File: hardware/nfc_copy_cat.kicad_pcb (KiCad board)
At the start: 2 copper layers, 40.4 x 43 mm, 39 parts, among them J1 USB_B_Micro, J2 Battery, J3 SWD, J4 NFC Module V3, J5 Conn_01x02, J6 Adafruit NFC 1.0, SW2 Magspoof, SW3 NFC, U1 AP2112K-3.3TRG1, U2 MCP73831-2-OT, U3 TC4424, U4 ATSAMD21E18A

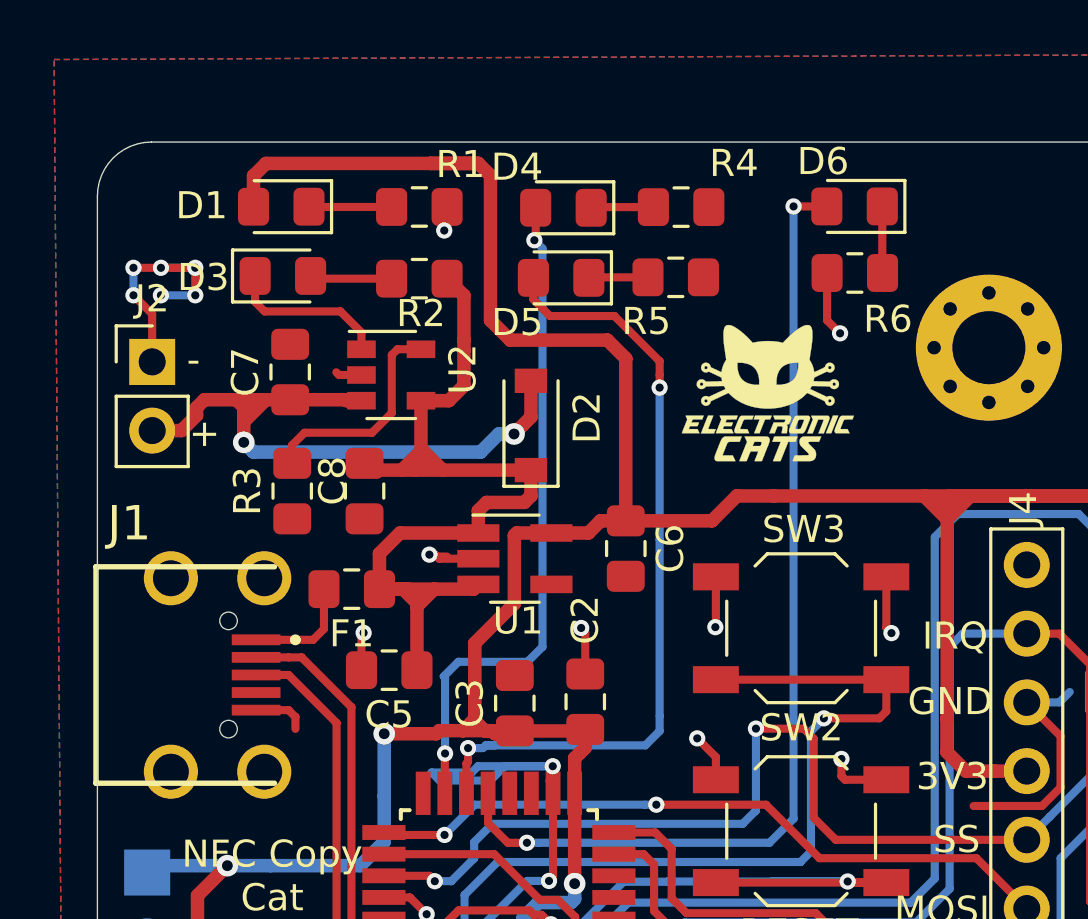
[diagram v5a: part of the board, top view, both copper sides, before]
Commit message: best labels description
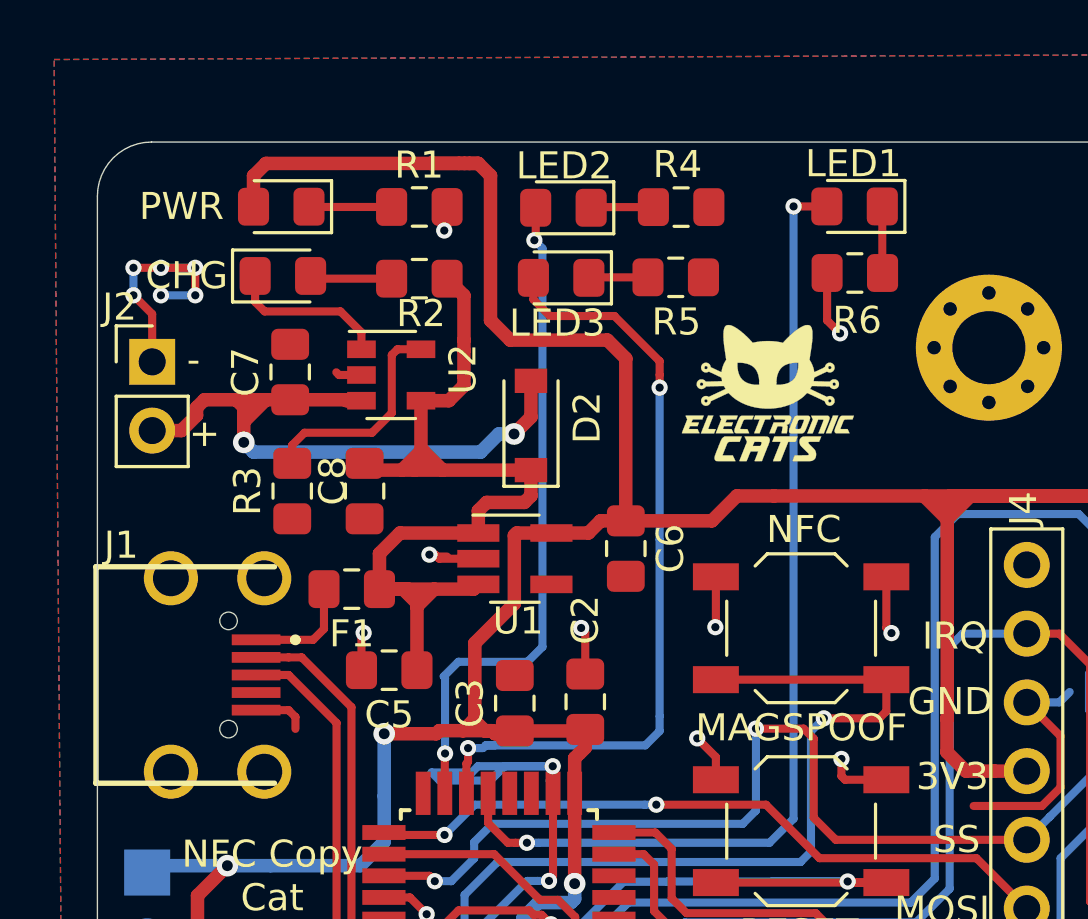
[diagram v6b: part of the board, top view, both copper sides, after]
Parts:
- renumbered D3 to CHG, D6 to LED1, D4 to LED2, D5 to LED3, SW2 to MAGSPOOF, SW3 to NFC, D1 to PWR
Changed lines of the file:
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@@
     (tags "SPST Tactile Switch")
     (attr smd)
-    (fp_text reference SW2 (at -0.01 3.82) (layer F.SilkS)
+    (fp_text reference MAGSPOOF (at -0.01 3.82) (layer F.SilkS)
       (effects (font (size 1 1) (thickness 0.15)))
     )
@@
     (descr U254-051N-4BH806-2)
     (tags Connector)
-    (fp_text reference J1 (at -5.6007 2.5019) (layer F.SilkS)
-      (effects (font (size 1.27 1.27) (thickness 0.254)))
+    (fp_text reference J1 (at -4.7975 2.8015) (layer F.SilkS)
+      (effects (font (size 1 1) (thickness 0.15)))
     )
     (fp_text value USB_B_Micro (at 0 -6.7 270) (layer F.SilkS) hide
@@
     (tags "SPST Tactile Switch")
     (attr smd)
-    (fp_text reference SW3 (at -0.1 3.65 180) (layer F.SilkS)
+    (fp_text reference NFC (at -0.1 3.65 180) (layer F.SilkS)
       (effects (font (size 1 1) (thickness 0.15)))
     )
@@
     (tags "LED handsolder")
     (attr smd)
-    (fp_text reference D1 (at 2.941 0.038) (layer F.SilkS)
+    (fp_text reference PWR (at 3.685 0.01) (layer F.SilkS)
       (effects (font (size 1 1) (thickness 0.15)))
     )
@@
     (tags "LED handsolder")
     (attr smd)
-    (fp_text reference D3 (at -2.941 0.056) (layer F.SilkS)
+    (fp_text reference CHG (at -3.555 -0.01) (layer F.SilkS)
       (effects (font (size 1 1) (thickness 0.15)))
     )
@@
     (descr "Through hole straight pin header, 1x02, 2.54mm pitch, single row")
     (tags "Through hole pin header THT 1x02 2.54mm single row")
-    (fp_text reference J2 (at 0 -2.33) (layer F.SilkS)
+    (fp_text reference J2 (at -1.205 -2.025) (layer F.SilkS)
       (effects (font (size 1 1) (thickness 0.15)))
     )
@@
     (tags "resistor handsolder")
     (attr smd)
-    (fp_text reference R1 (at 1.52 -1.57) (layer F.SilkS)
+    (fp_text reference R1 (at -0.01 -1.55) (layer F.SilkS)
       (effects (font (size 1 1) (thickness 0.15)))
     )
@@
     (tags "LED handsolder")
     (attr smd)
-    (fp_text reference D4 (at 1.715 1.5) (layer F.SilkS)
+    (fp_text reference LED2 (at -0.025 1.55) (layer F.SilkS)
       (effects (font (size 1 1) (thickness 0.15)))
     )
@@
     (tags "resistor handsolder")
     (attr smd)
-    (fp_text reference R4 (at 1.954999 -1.615001) (layer F.SilkS)
+    (fp_text reference R4 (at -0.135001 -1.575001) (layer F.SilkS)
       (effects (font (size 1 1) (thickness 0.15)))
     )
@@
     (tags "LED handsolder")
     (attr smd)
-    (fp_text reference D5 (at 1.62 -1.65) (layer F.SilkS)
+    (fp_text reference LED3 (at 0.14 -1.67) (layer F.SilkS)
       (effects (font (size 1 1) (thickness 0.15)))
     )
@@
     (tags "LED handsolder")
     (attr smd)
-    (fp_text reference D6 (at 1.165 1.66) (layer F.SilkS)
+    (fp_text reference LED1 (at 0.045 1.58) (layer F.SilkS)
       (effects (font (size 1 1) (thickness 0.15)))
     )
@@
     (tags "resistor handsolder")
     (attr smd)
-    (fp_text reference R5 (at -1.085 1.63) (layer F.SilkS)
+    (fp_text reference R5 (at 0.025 1.65) (layer F.SilkS)
       (effects (font (size 1 1) (thickness 0.15)))
     )
@@
     (tags "resistor handsolder")
     (attr smd)
-    (fp_text reference R6 (at -1.225 -1.71) (layer F.SilkS)
-      (effects (font (size 1 1) (thickness 0.15)))
-    )
+    (fp_text reference R6 (at -0.085 -1.75) (layer F.SilkS)
+      (effects (font (size 1 1) (thickness 0.15)))
+    )

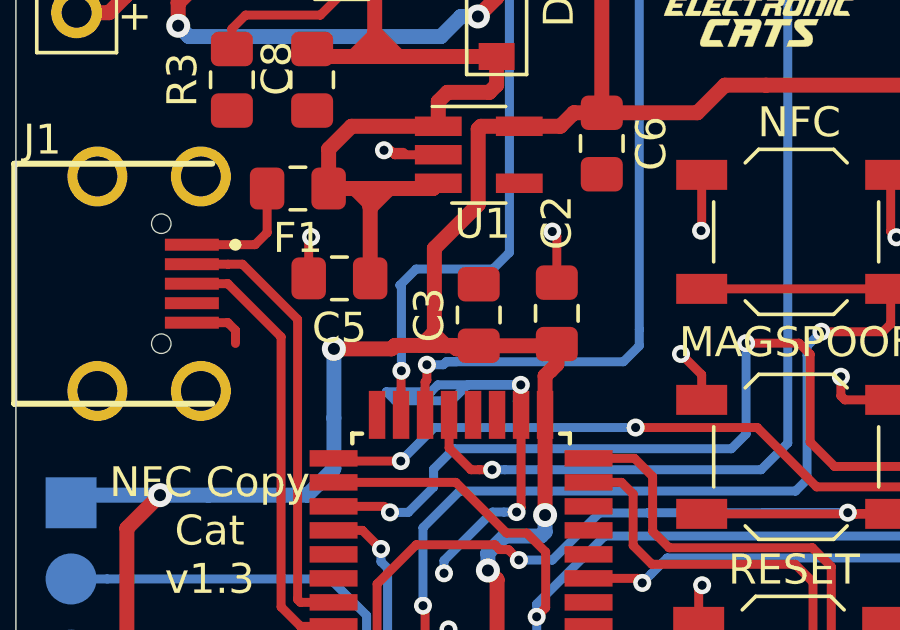
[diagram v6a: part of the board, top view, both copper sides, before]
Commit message: remove c3
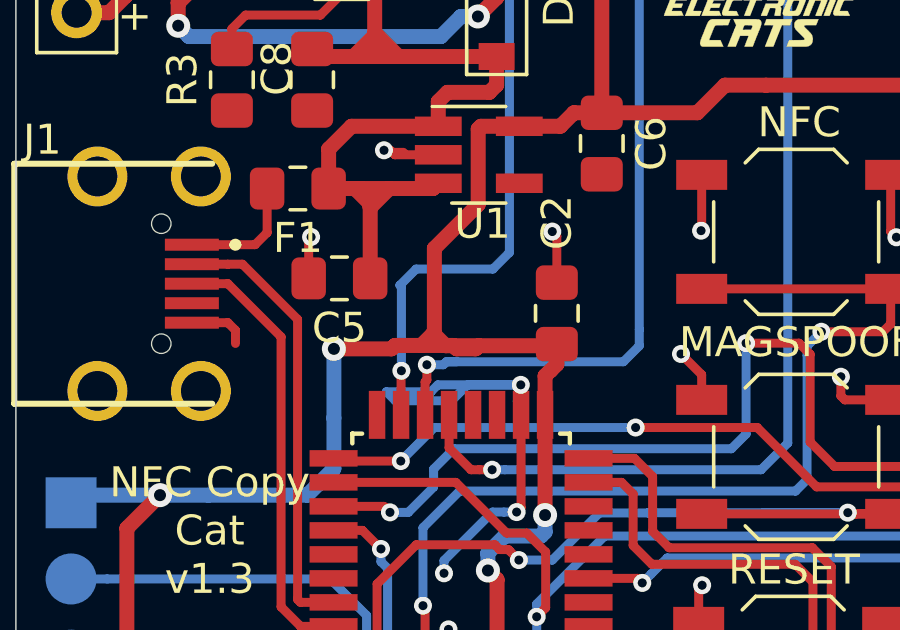
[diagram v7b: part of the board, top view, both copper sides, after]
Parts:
- removed C3: 0.1uf, Capacitor_SMD:C_0805_2012Metric_Pad1.15x1.40mm_HandSolder
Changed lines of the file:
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@@
     (tracks 597)
     (zones 0)
-    (modules 39)
+    (modules 38)
     (nets 49)
   )
@@
       (drillshape 0)
       (scaleselection 1)
-      (outputdirectory "gerbers_nfc/"))
+      (outputdirectory "gerbers_nfc1v3/"))
   )
   (net 0 "")
@@
     (model ${KISYS3DMOD}/Capacitor_SMD.3dshapes/C_0805_2012Metric.wrl
       (at (xyz 0 0 0))
-      (scale (xyz 1 1 1))
-      (rotate (xyz 0 0 0))
-    )
-  )
-  (module Capacitor_SMD:C_0805_2012Metric_Pad1.15x1.40mm_HandSolder (layer F.Cu)
-    (at 143.128 69.941 90)
-    (descr "Capacitor SMD 0805 (2012 Metric), square (rectangular) end terminal, IPC_7351 nominal with elongated pad for handsoldering. (Body size source: https://docs.google.com/spreadsheets/d/1BsfQQcO9C6DZCsRaXUlFlo91Tg2WpOkGARC1WS5S8t0/edit?usp=sharing), generated with kicad-footprint-generator")
-    (tags "capacitor handsolder")
-    (attr smd)
-    (fp_text reference C3 (at 0 -1.65 90) (layer F.SilkS)
-      (effects (font (size 1 1) (thickness 0.15)))
-    )
-    (fp_text value 0.1uf (at 0 1.65 90) (layer F.Fab)
-      (effects (font (size 1 1) (thickness 0.15)))
-    )
-    (fp_line (start -1 0.6) (end -1 -0.6) (layer F.Fab) (width 0.1))
-    (fp_line (start -1 -0.6) (end 1 -0.6) (layer F.Fab) (width 0.1))
-    (fp_line (start 1 -0.6) (end 1 0.6) (layer F.Fab) (width 0.1))
-    (fp_line (start 1 0.6) (end -1 0.6) (layer F.Fab) (width 0.1))
-    (fp_line (start -0.261252 -0.71) (end 0.261252 -0.71) (layer F.SilkS) (width 0.12))
-    (fp_line (start -0.261252 0.71) (end 0.261252 0.71) (layer F.SilkS) (width 0.12))
-    (fp_line (start -1.85 0.95) (end -1.85 -0.95) (layer F.CrtYd) (width 0.05))
-    (fp_line (start -1.85 -0.95) (end 1.85 -0.95) (layer F.CrtYd) (width 0.05))
-    (fp_line (start 1.85 -0.95) (end 1.85 0.95) (layer F.CrtYd) (width 0.05))
-    (fp_line (start 1.85 0.95) (end -1.85 0.95) (layer F.CrtYd) (width 0.05))
-    (fp_text user %R (at 0 0 90) (layer F.Fab)
-      (effects (font (size 0.5 0.5) (thickness 0.08)))
-    )
-    (pad 1 smd roundrect (at -1.025 0 90) (size 1.15 1.4) (layers F.Cu F.Paste F.Mask) (roundrect_rratio 0.217391)
-      (net 1 +3V3))
-    (pad 2 smd roundrect (at 1.025 0 90) (size 1.15 1.4) (layers F.Cu F.Paste F.Mask) (roundrect_rratio 0.217391)
-      (net 2 GND))
-    (model ${KISYS3DMOD}/Capacitor_SMD.3dshapes/C_0805_2012Metric.wrl
-      (at (xyz 0 0 0))

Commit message: netlist
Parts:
- added C3: 0.1uF, Capacitor_SMD:C_0805_2012Metric_Pad1.15x1.40mm_HandSolder, F.Cu at (200.2, 91.1)
- added R7: 100K, Resistor_SMD:R_0805_2012Metric_Pad1.15x1.40mm_HandSolder, F.Cu at (200.2, 94.1)
- added U5: W25Q16JVSS, Package_SO:SOIC-8_5.23x5.23mm_P1.27mm, F.Cu at (192.6, 93.1)
- renumbered PWR to D1, CHG to D3, LED2 to D4, LED3 to D5, LED1 to D6, RESET to SW1, MAGSPOOF to SW2, NFC to SW3
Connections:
- J3 pad 1: +3V3 -> GND
- J3 pad 2: /SWDIO -> /SWCLK
- J3 pad 3: /SWCLK -> /SWDIO
- J3 pad 4: GND -> +3V3
- U4 pad 11: Net-(U4-Pad11) -> /MOSI
- U4 pad 12: Net-(U4-Pad12) -> /SCK
- U4 pad 13: /LED3 -> /SS
- U4 pad 14: /LED2 -> /MISO
- U4 pad 5: Net-(U4-Pad5) -> /LED3
- U4 pad 6: Net-(U4-Pad6) -> /LED2
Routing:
- net +3V3: track 163.5 -> 0.00 mm, vias 4 -> 0
- net GND: track 87.0 -> 0.91 mm, vias 29 -> 1
- net /12(MISO): track 73.3 -> 0.00 mm, vias 3 -> 0
- net /13(SCK): track 65.3 -> 0.00 mm, vias 1 -> 0
- net /11(MOSI): track 40.4 -> 0.00 mm, vias 2 -> 0
- net /IRQ: track 38.5 -> 0.00 mm, vias 1 -> 0
- net /LED3: track 36.9 -> 0.00 mm, vias 2 -> 0
- net /10(SS): track 36.6 -> 0.00 mm, vias 2 -> 0
- net VCC: track 35.2 -> 0.00 mm
- net /SW2: track 33.2 -> 0.00 mm, vias 2 -> 0
- net /SW1: track 30.5 -> 0.00 mm, vias 2 -> 0
- net /LED2: track 29.5 -> 0.00 mm, vias 2 -> 0
- net /RESET: track 27.8 -> 0.00 mm, vias 3 -> 0
- net /SWDIO: track 26.0 -> 0.00 mm, vias 1 -> 0
- net /SWCLK: track 25.0 -> 0.00 mm, vias 1 -> 0
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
